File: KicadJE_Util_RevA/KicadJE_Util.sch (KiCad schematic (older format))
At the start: 121 parts, among them J101 Out1, J102 Out2, J103 SawOut3, J104 In1.1, J105 In1.2, J106 In1.3, J107 SS_In2, J111 SineOut4, P101 HEADER_2x5_Doepfer, Q101 MMBT3906, Q102 UMX1N, SW101 Octave (3 state), U101 TL072, U102 TL072, U103 TL072, U105 L78L05_SOT89, U106 L79L05_SOT89, U107 TL072

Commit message: Base sch done
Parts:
- removed C107: 220p, Capacitor_SMD:C_0805_2012Metric_Pad1.15x1.40mm_HandSolder, symbol Device:C
- removed C108, C109, C116, C117: 100n, Capacitor_SMD:C_0805_2012Metric_Pad1.15x1.40mm_HandSolder, symbol Device:C
- removed C110: 1n poly, Capacitor_THT:C_Rect_L7.0mm_W2.0mm_P5.00mm, symbol Device:C
- removed C111: 1n alt, Capacitor_SMD:C_0805_2012Metric_Pad1.15x1.40mm_HandSolder, symbol Device:C
- removed D115: Germanium, Diode_THT:D_A-405_P7.62mm_Horizontal, symbol Device:D
- removed D117, D118: 1N1007, Diode_SMD:D_SOD-123, symbol Device:D
- removed J103: SawOut3, AJ-Dropbox-Kicad:PJ301SM, symbol Connector:AudioJack2_SwitchT
- removed J111: SineOut4, AJ-Dropbox-Kicad:PJ301SM, symbol Connector:AudioJack2_SwitchT
- removed JP101: Jumper_3_Bridged12, Jumper:SolderJumper-3_P1.3mm_Bridged12_Pad1.0x1.5mm_NumberLabels, symbol Jumper:Jumper_3_Bridged12
- removed Q101: MMBT3906, Package_TO_SOT_SMD:SOT-23, symbol Transistor_BJT:MMBT3906
- removed Q102: UMX1N, AJ:UMX1N_UMT6_DualNPN, symbol UMX1N:UMX1N
- removed R101, R135, R136, R137: 47k, Resistor_SMD:R_0805_2012Metric_Pad1.15x1.40mm_HandSolder, symbol Device:R
- removed R102: 470R, Resistor_SMD:R_0805_2012Metric_Pad1.15x1.40mm_HandSolder, symbol Device:R
- removed R103: 82k, Resistor_SMD:R_0805_2012Metric_Pad1.15x1.40mm_HandSolder, symbol Device:R
- removed R104: 20k, Resistor_SMD:R_0805_2012Metric_Pad1.15x1.40mm_HandSolder, symbol Device:R
- removed R107, R153, R155: 1k, Resistor_SMD:R_0805_2012Metric_Pad1.15x1.40mm_HandSolder, symbol Device:R
- removed R133, R156: 100k, Resistor_SMD:R_0805_2012Metric_Pad1.15x1.40mm_HandSolder, symbol Device:R
- removed R139, R147: 2k20, Resistor_SMD:R_0805_2012Metric_Pad1.15x1.40mm_HandSolder, symbol Device:R
- removed R140, R143, R158, R161: 10k, Resistor_SMD:R_0805_2012Metric_Pad1.15x1.40mm_HandSolder, symbol Device:R
- removed R141: 390R, Resistor_SMD:R_0805_2012Metric_Pad1.15x1.40mm_HandSolder, symbol Device:R
- removed R142: 18k, Resistor_SMD:R_0805_2012Metric_Pad1.15x1.40mm_HandSolder, symbol Device:R
- removed R144: 26k7, Resistor_SMD:R_0805_2012Metric_Pad1.15x1.40mm_HandSolder, symbol Device:R
- removed R145: 6k04, Resistor_SMD:R_0805_2012Metric_Pad1.15x1.40mm_HandSolder, symbol Device:R
- removed R146: 1M2, Resistor_SMD:R_0805_2012Metric_Pad1.15x1.40mm_HandSolder, symbol Device:R
- removed R148: 1k82, Resistor_SMD:R_0805_2012Metric_Pad1.15x1.40mm_HandSolder, symbol Device:R
- removed R149, R150: 13k3, Resistor_SMD:R_0805_2012Metric_Pad1.15x1.40mm_HandSolder, symbol Device:R
- removed R151, R163: OPEN, Resistor_SMD:R_0805_2012Metric_Pad1.15x1.40mm_HandSolder, symbol Device:R
- removed R152: 0R, Resistor_SMD:R_0805_2012Metric_Pad1.15x1.40mm_HandSolder, symbol Device:R
- removed R154: 3k, Resistor_SMD:R_0805_2012Metric_Pad1.15x1.40mm_HandSolder, symbol Device:R
- removed R157: 15k, Resistor_SMD:R_0805_2012Metric_Pad1.15x1.40mm_HandSolder, symbol Device:R
- removed R160, R162: 25k, Resistor_SMD:R_0805_2012Metric_Pad1.15x1.40mm_HandSolder, symbol Device:R
- removed RV101: 100k Fine, AJ-Dropbox-Kicad:Potentiometer_China_RK09_Single_Vertical_AJ, symbol Envelope-cache-2018-08-04-13-00-04:POT
- removed RV103: 5k, Potentiometer_THT:Potentiometer_Bourns_3296W_Vertical, symbol Device:R_POT_TRIM
- removed RV104: 50k, Potentiometer_THT:Potentiometer_Bourns_3296W_Vertical, symbol Device:R_POT_TRIM
- removed SW101: Octave (3 state), AJ-Dropbox-Kicad:SP1MS1, symbol Switch:SW_SPDT
- removed TP101: Oct, AJ:Pot_6m3, symbol Connector:TestPoint
- removed TP115: 3m5 jack, AJ:Jack_6m3, symbol Connector:TestPoint
- removed U102: TL072, AJ-Dropbox-Kicad:AJ_SO-8_5.3x6.2mm_P1.27mm, symbol Amplifier_Operational:TL072
- removed unit 2 of U103
- removed unit 1 of U103
- removed U105: L78L05_SOT89, Package_TO_SOT_SMD:SOT-89-3, symbol Regulator_Linear:L78L05_SOT89
- removed U106: L79L05_SOT89, Package_TO_SOT_SMD:SOT-89-3, symbol Regulator_Linear:L79L05_SOT89
- removed unit 3 of U107
- added R113, R115, R116: 10k, Resistor_SMD:R_0805_2012Metric_Pad1.15x1.40mm_HandSolder, symbol Device:R
- added R118, R120, R129: 20k, Resistor_SMD:R_0805_2012Metric_Pad1.15x1.40mm_HandSolder, symbol Device:R
- added R124, R125, R126: 1k, Resistor_SMD:R_0805_2012Metric_Pad1.15x1.40mm_HandSolder, symbol Device:R
- added RV102: 100k Gain1, AJ-Dropbox-Kicad:Potentiometer_China_RK09_Single_Vertical_AJ, symbol Envelope-cache-2018-08-04-13-00-04:POT
- added RV103: 100k Gain2, AJ-Dropbox-Kicad:Potentiometer_China_RK09_Single_Vertical_AJ, symbol Envelope-cache-2018-08-04-13-00-04:POT
- added RV104: 100k Offset2, AJ-Dropbox-Kicad:Potentiometer_China_RK09_Single_Vertical_AJ, symbol Envelope-cache-2018-08-04-13-00-04:POT
- added TP108: OFF2, AJ:Pot_6m3_scale1, symbol Connector:TestPoint
- added TP109: Gain2, AJ:Pot_6m3_scale1, symbol Connector:TestPoint
- added TP110: Gain1, AJ:Pot_6m3_scale1, symbol Connector:TestPoint
- R114: value 1k6 -> 10k
- R119: value 1M -> 20k
- R121, R128: value 12k5 -> 20k
- R127, R131: value 10k -> 1k
- R130: renamed from R159; value 10k -> 1k
- RV101: renamed from RV102; value 100k PWM -> 100k Offset1
- TP107: renamed from TP113; value PWM -> OFF1
- TP111: value Saw -> Flow1; footprint AJ:Jack_6m3 -> TestPoint:TestPoint_THTPad_2.0x2.0mm_Drill1.0mm
- TP112: value Fine -> Flow2; footprint AJ:Pot_6m3_scale1 -> TestPoint:TestPoint_THTPad_2.0x2.0mm_Drill1.0mm
- gave numbers to parts that had none: 13
- renumbered C112 to C101, C113 to C102, C114 to C103, C115 to C104, C118 to C105, C119 to C106, D113 to D101, D114 to D102, D116 to D103, D105 to D107, D107 to D111, H105 to H101, H101 to H102, H102 to H103, H103 to H104, H104 to H105, J104 to J103, J105 to J104, J106 to J105, J107 to J106, R138 to R101, R106 to R103, R105 to R104, R116 to R105, R110 to R109, R120 to R117, R126 to R122, R130 to R123, TP109 to TP101, TP110 to TP102, TP102 to TP103, TP103 to TP104, TP104 to TP105, TP105 to TP106, U103 to U102, U107 to U102
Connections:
- net labels added: Flow1, Flow2
- net labels removed: +5V, -5V, 3CVIn1, 3FM_Lin_In4, 3HardSyncIn3, 3Octave, 3PWM_Adj, 3PWM_In5, 3Sine, 3SoftSyncIn2, 3VP_2, 3VSO_3, 3VTO_1
- wire segments 387 -> 219
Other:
- note added: "NonInv/Inv Input"
- note removed: "1n timing cap\n0805 as backup\nTHT 1000 pf poly"
- note removed: "Freq Manual Adjust"
- note removed: "Octave Adjust"
- note removed: "PWM Manual Adjust"
- note removed: "Prophet 5"
- note removed: "Prophet T8"
- moved on the sheet: C101, C102, C103, C104, C105, C106, D101, D102, D103, D104, D105, D106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

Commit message: fix flow
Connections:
- net Flow1: now also R111.1
- net Flow2: now also R122.1
- net Out1: no longer R111.1
- net Out2: no longer R122.1
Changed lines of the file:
@@
 	4475 7450 4925 7450
 Text GLabel 3525 7575 2    50   Input ~ 0
-Out1
+Flow1
 Text GLabel 6500 7550 2    50   Input ~ 0
-Out2
+Flow2
 Wire Wire Line
 	2975 7575 3525 7575

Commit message: Timeshift Added
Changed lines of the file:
@@
 $Descr A4 11693 8268
 encoding utf-8
-Sheet 1 2
+Sheet 1 3
 Title "Kicad JE - Util"
 Date "2020-03-17"
@@
 Wire Notes Line
 	4500 4100 8450 4100
+$Sheet
+S 9000 4250 1750 2025
+U 5EFABE3E
+F0 "KicadJE_Timeshift_Mini" 50
+F1 "KicadJE_Timeshift_Mini.sch" 50
+$EndSheet
 $EndSCHEMATC

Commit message: ERC
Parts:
- R126, R127: value 1k -> OPEN
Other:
- note added: "CHECK POTS"
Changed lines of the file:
@@
 AR Path="/5F49A670/5FC025E5" Ref="R?"  Part="1"
 F 0 "R126" V 6375 5075 50  0000 C CNN
-F 1 "1k" V 6475 5150 50  0000 C CNN
+F 1 "OPEN" V 6475 5150 50  0000 C CNN
 F 2 "Resistor_SMD:R_0805_2012Metric_Pad1.15x1.40mm_HandSolder" V 6405 5150 50  0001 C CNN
 F 3 "~" H 6475 5150 50  0001 C CNN
@@
 AR Path="/5F49A670/5FC820A2" Ref="R?"  Part="1"
 F 0 "R127" V 6375 6075 50  0000 C CNN
-F 1 "1k" V 6475 6150 50  0000 C CNN
+F 1 "OPEN" V 6475 6150 50  0000 C CNN
 F 2 "Resistor_SMD:R_0805_2012Metric_Pad1.15x1.40mm_HandSolder" V 6405 6150 50  0001 C CNN
 F 3 "~" H 6475 6150 50  0001 C CNN
@@
 F1 "KicadJE_Timeshift_Mini.sch" 50
 $EndSheet
+Text Notes 3900 6875 0    97   ~ 0
+CHECK POTS
+Text Notes 7450 5200 0    97   ~ 0
+CHECK POTS
 $EndSCHEMATC

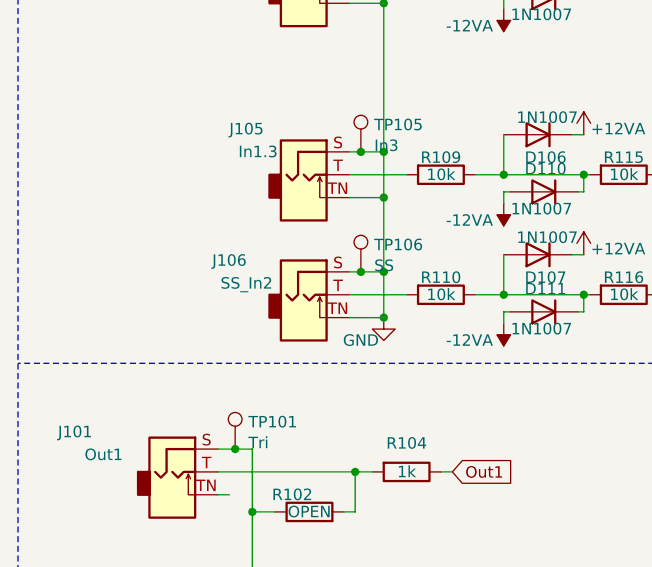
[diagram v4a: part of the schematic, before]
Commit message: Faceplace komp placed
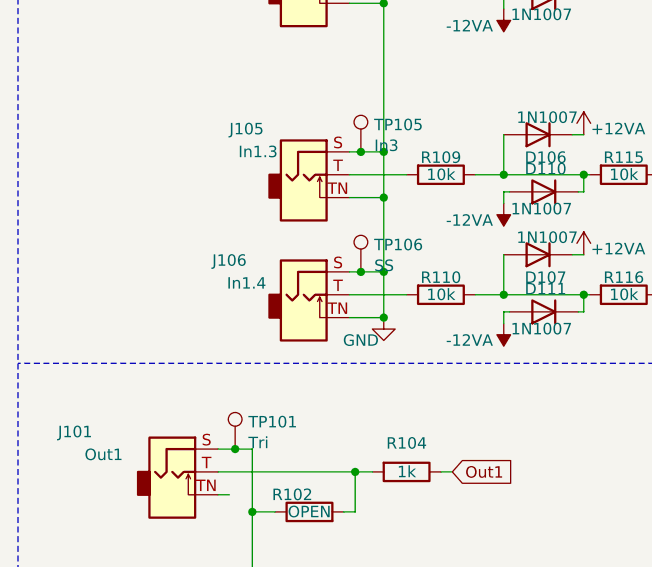
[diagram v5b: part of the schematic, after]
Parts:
- J106: value SS_In2 -> In1.4
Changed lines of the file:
@@
 AR Path="/5F49A670/5F4B92A3" Ref="J?"  Part="1"
 F 0 "J106" H 1450 4700 50  0000 C CNN
-F 1 "SS_In2" H 1525 4600 50  0000 C CNN
+F 1 "In1.4" H 1525 4600 50  0000 C CNN
 F 2 "AJ-Dropbox-Kicad:PJ301SM" H 1775 4550 50  0001 C CNN
 F 3 "~" H 1775 4550 50  0001 C CNN

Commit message: CV Module placed
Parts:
- renumbered U102 to U101, U101 to U102
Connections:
- net +12VA: now also RV101.1, RV104.1; no longer RV101.3, RV104.3
- net -12VA: now also RV101.3, RV104.3; no longer RV101.1, RV104.1
- net In2: now also U102.3 (+); no longer U102.5 (+)
- net Inv2: now also RV103.1, U102.2 (-); no longer RV103.3, U102.6 (-)
- net Out2: now also U102.7; no longer U102.1
- net at R127.1, R129.1: now also RV103.3; no longer RV103.1
- net at R129.2, R131.2: now also U102.1; no longer U102.7
- net at R117.1, R123.2: now also U102.6 (-); no longer U102.2 (-)
- net at R122.2: now also U102.5 (+); no longer U102.3 (+)
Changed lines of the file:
@@
 $Comp
 L Amplifier_Operational:TL072 U?
-U 1 1 5FD1A01E
+U 2 1 5FD1A01E
 P 5275 7450
 AR Path="/5D99B81E/5FD1A01E" Ref="U?"  Part="3"
@@
 AR Path="/5E62ACA1/5FD1A01E" Ref="U?"  Part="1"
 AR Path="/5F49A670/5FD1A01E" Ref="U?"  Part="1"
-AR Path="/5FD1A01E" Ref="U101"  Part="1"
-F 0 "U101" H 5275 7400 50  0000 C CNN
+AR Path="/5FD1A01E" Ref="U102"  Part="2"
+F 0 "U102" H 5275 7400 50  0000 C CNN
 F 1 "TL072" H 5225 7475 50  0000 C CNN
 F 2 "AJ-Dropbox-Kicad:AJ_SO-8_5.3x6.2mm_P1.27mm" H 5275 7450 50  0001 C CNN
 F 3 "http://www.ti.com/lit/ds/symlink/tl071.pdf" H 5275 7450 50  0001 C CNN
-	1    5275 7450
+	2    5275 7450
 	-1   0    0    1
 $EndComp
@@
 AR Path="/5E62ACA1/604DA92D" Ref="U?"  Part="1"
 AR Path="/5F49A670/604DA92D" Ref="U?"  Part="1"
-AR Path="/604DA92D" Ref="U102"  Part="1"
-F 0 "U102" H 6225 4625 50  0000 C CNN
+AR Path="/604DA92D" Ref="U101"  Part="1"
+F 0 "U101" H 6225 4625 50  0000 C CNN
 F 1 "TL072" H 6250 4550 50  0000 C CNN
 F 2 "AJ-Dropbox-Kicad:AJ_SO-8_5.3x6.2mm_P1.27mm" H 6325 4600 50  0001 C CNN
@@
 $Comp
 L Amplifier_Operational:TL072 U?
-U 2 1 6058F368
+U 1 1 6058F368
 P 6325 5600
 AR Path="/5D99B81E/6058F368" Ref="U?"  Part="3"
@@
 AR Path="/5E62ACA1/6058F368" Ref="U?"  Part="1"
 AR Path="/5F49A670/6058F368" Ref="U?"  Part="2"
-AR Path="/6058F368" Ref="U102"  Part="2"
+AR Path="/6058F368" Ref="U102"  Part="1"
 F 0 "U102" H 6275 5600 50  0000 C CNN
 F 1 "TL072" H 6425 5450 50  0000 C CNN
 F 2 "AJ-Dropbox-Kicad:AJ_SO-8_5.3x6.2mm_P1.27mm" H 6325 5600 50  0001 C CNN
 F 3 "http://www.ti.com/lit/ds/symlink/tl071.pdf" H 6325 5600 50  0001 C CNN
-	2    6325 5600
+	1    6325 5600
 	1    0    0    -1
 $EndComp
@@
 F 3 "" H 3325 7100 50  0001 C CNN
 	1    3325 7100
-	-1   0    0    1
+	-1   0    0    -1
 $EndComp
 $Comp
@@
 AR Path="/5F49A670/5FA15097" Ref="RV?"  Part="1"
 AR Path="/5FA15097" Ref="RV104"  Part="1"
-F 0 "RV104" V 6300 7100 50  0000 C CNN
+F 0 "RV104" V 6300 7075 50  0000 C CNN
 F 1 "100k Offset2" V 6200 7075 50  0000 C CNN
 F 2 "AJ-Dropbox-Kicad:Potentiometer_China_RK09_Single_Vertical_AJ" H 6300 7075 50  0001 C CNN
 F 3 "" H 6300 7075 50  0001 C CNN
 	1    6300 7075
-	-1   0    0    1
+	-1   0    0    -1
 $EndComp
 $Comp
@@
 F 3 "" H 6275 6000 50  0001 C CNN
 	1    6275 6000
-	0    1    1    0
+	0    -1   1    0
 $EndComp
 $Comp
@@
 	8450 525  8450 6525
 $Sheet
-S 4700 1475 1750 1775
+S 4675 1475 1775 1750
 U 5FDBD837
 F0 "KicadJE_Util_CV2" 50
